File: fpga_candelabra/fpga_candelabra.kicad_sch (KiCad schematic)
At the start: 0 parts

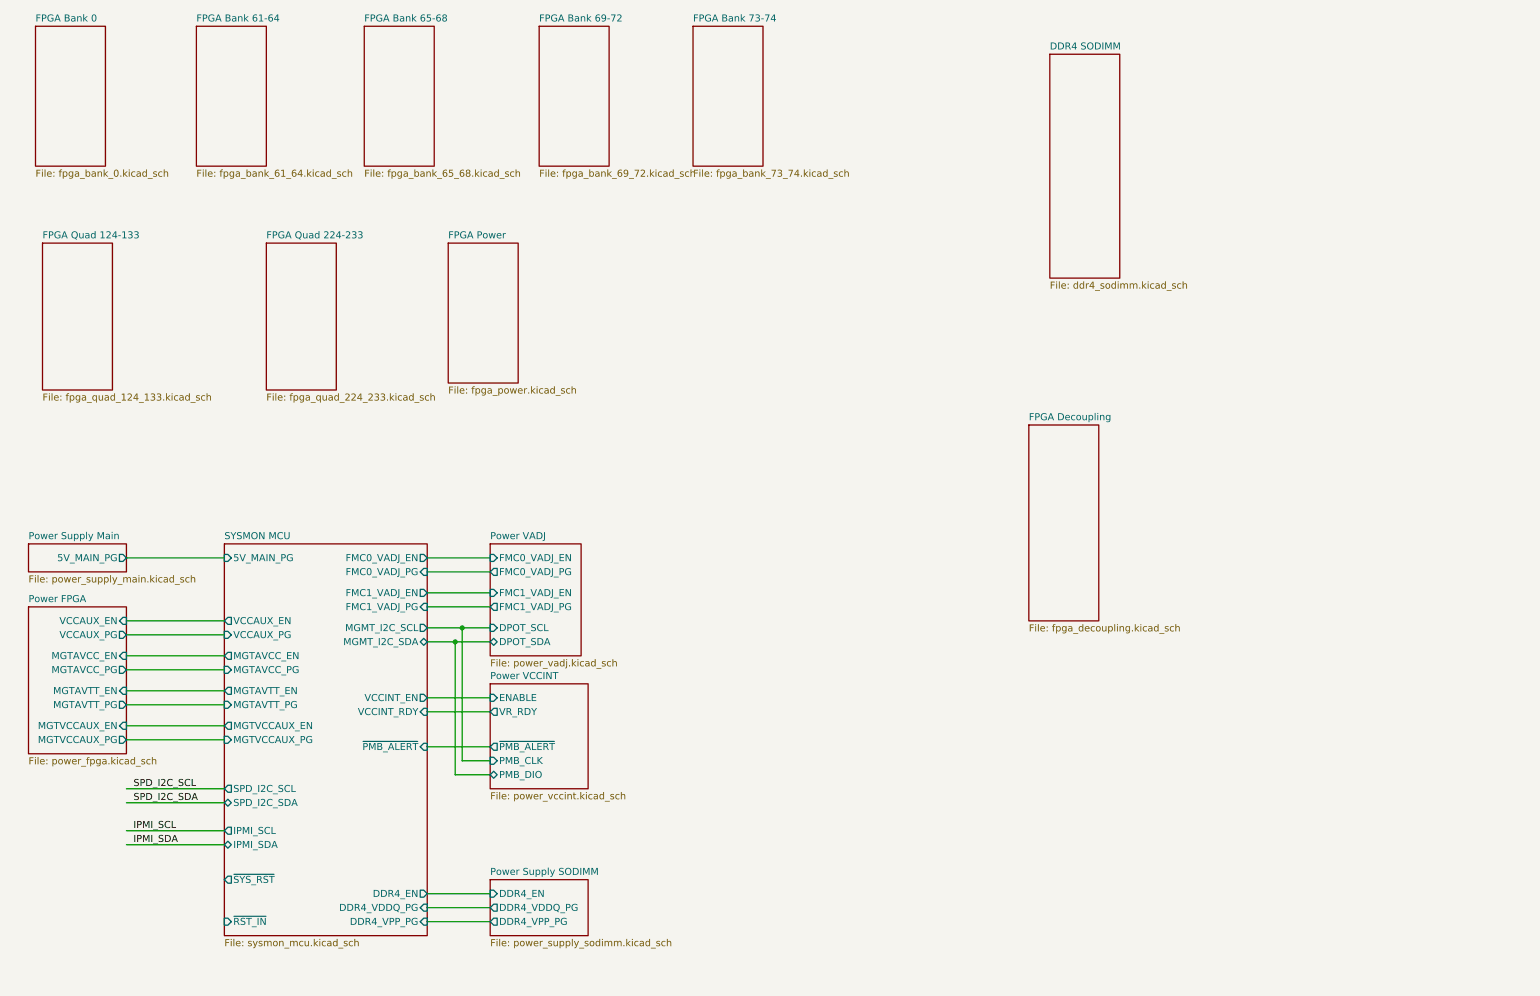
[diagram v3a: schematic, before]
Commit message: fpga_candelabra: reorganize fpga io and mgt by SLR
- Rename sch sheets
- Add prelimary DDR and PCIE Bank/Quad allocation

Signed-off-by: Yichuan Gao <gaoyichuan000@gmail.com>
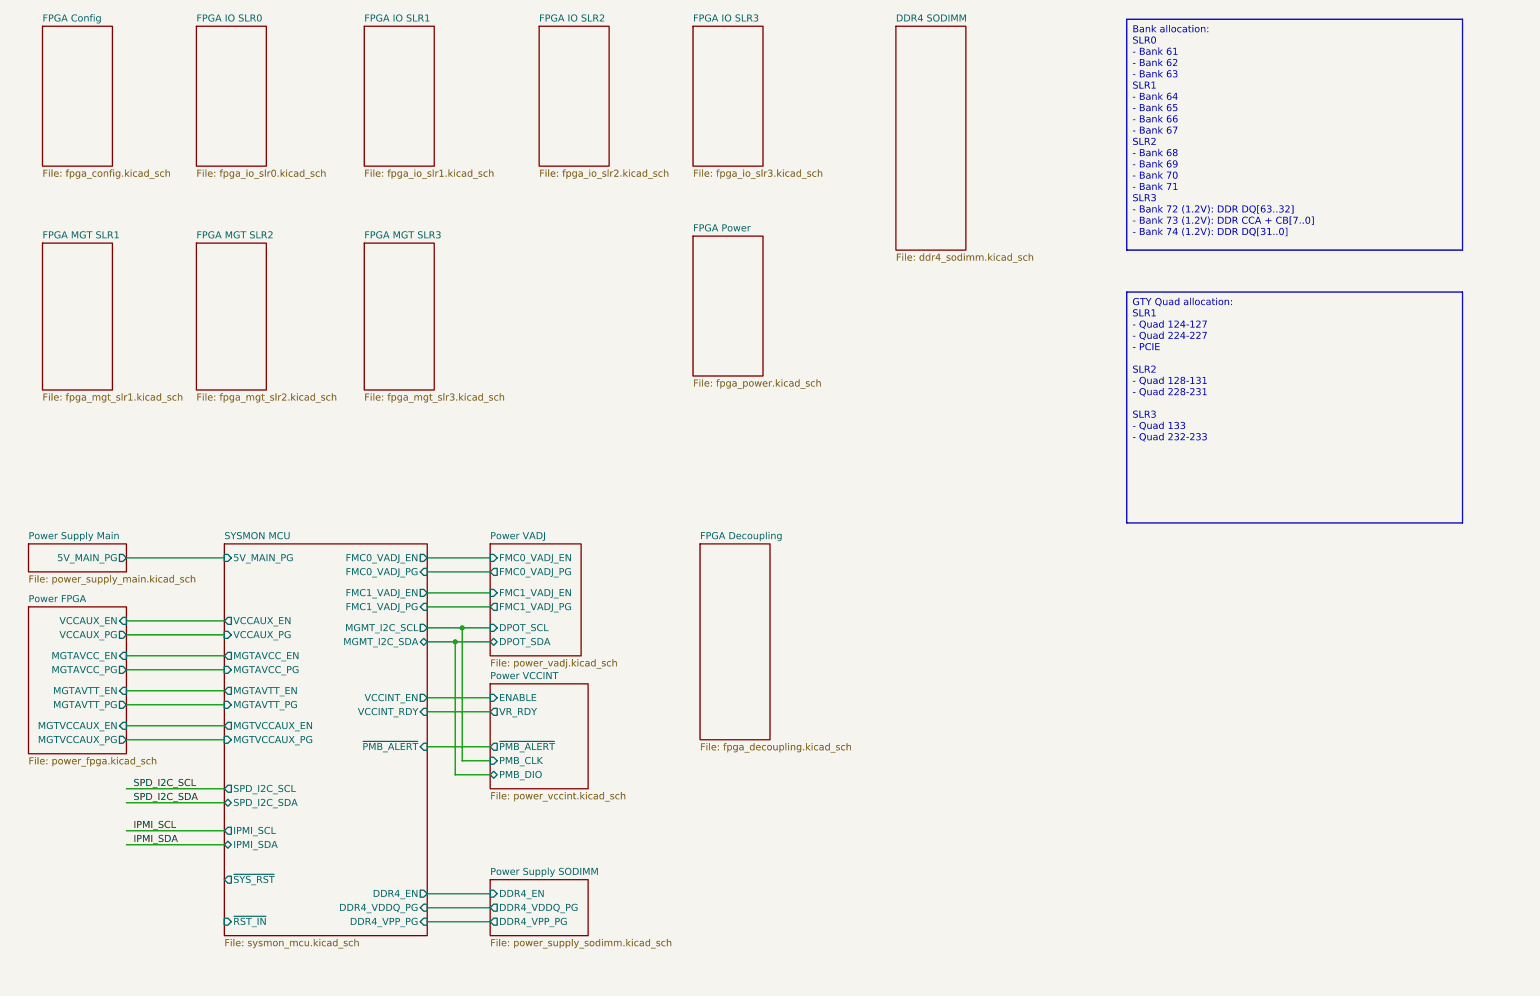
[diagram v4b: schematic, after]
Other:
- sheet FPGA Bank 0 renamed FPGA Config
- sheet FPGA Bank 61-64 renamed FPGA IO SLR0
- sheet FPGA Bank 65-68 renamed FPGA IO SLR1
- sheet FPGA Bank 69-72 renamed FPGA IO SLR2
- sheet FPGA Bank 73-74 renamed FPGA IO SLR3
- sheet FPGA Quad 124-133 renamed FPGA MGT SLR1
- sheet FPGA Quad 224-233 renamed FPGA MGT SLR2
- added sheet FPGA MGT SLR3 (fpga_mgt_slr3.kicad_sch)
- sheet FPGA Config: file fpga_bank_0.kicad_sch -> fpga_config.kicad_sch
- sheet FPGA IO SLR0: file fpga_bank_61_64.kicad_sch -> fpga_io_slr0.kicad_sch
- sheet FPGA IO SLR1: file fpga_bank_65_68.kicad_sch -> fpga_io_slr1.kicad_sch
- sheet FPGA IO SLR2: file fpga_bank_69_72.kicad_sch -> fpga_io_slr2.kicad_sch
- sheet FPGA IO SLR3: file fpga_bank_73_74.kicad_sch -> fpga_io_slr3.kicad_sch
- sheet FPGA MGT SLR1: file fpga_quad_124_133.kicad_sch -> fpga_mgt_slr1.kicad_sch
- sheet FPGA MGT SLR2: file fpga_quad_224_233.kicad_sch -> fpga_mgt_slr2.kicad_sch
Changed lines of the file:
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@@
 		)
 	)
-	(label "SPD_I2C_SDA"
-		(at 39.37 161.29 0)
-		(fields_autoplaced yes)
+	(text_box "Bank allocation:\nSLR0\n  - Bank 61\n  - Bank 62\n  - Bank 63\nSLR1\n  - Bank 64\n  - Bank 65\n  - Bank 66\n  - Bank 67\nSLR2\n  - Bank 68\n  - Bank 69\n  - Bank 70\n  - Bank 71\nSLR3\n  - Bank 72 (1.2V): DDR DQ[63..32]\n  - Bank 73 (1.2V): DDR CCA + CB[7..0]\n  - Bank 74 (1.2V): DDR DQ[31..0]"
+		(exclude_from_sim no)
+		(at 219.71 19.05 0)
+		(size 60.96 41.91)
+		(stroke
+			(width 0)
+			(type default)
+		)
+		(fill
+			(type none)
+		)
 		(effects
 			(font
 				(size 1.27 1.27)
 			)
-			(justify left bottom)
-		)
-	)
-	(label "IPMI_SCL"
-		(at 39.37 166.37 0)
-		(fields_autoplaced yes)
+			(justify left top)
+		)
+	)
+	(text_box "GTY Quad allocation:\nSLR1\n  - Quad 124-127\n  - Quad 224-227\n    - PCIE\n\nSLR2\n  - Quad 128-131\n  - Quad 228-231\n\nSLR3\n  - Quad 133\n  - Quad 232-233"
+		(exclude_from_sim no)
+		(at 219.71 68.58 0)
+		(size 60.96 41.91)
+		(stroke
+			(width 0)
+			(type default)
+		)
+		(fill
+			(type none)
+		)
 		(effects
 			(font
 				(size 1.27 1.27)
 			)
-			(justify left bottom)
-		)
-	)
-	(label "SPD_I2C_SCL"
-		(at 39.37 158.75 0)
+			(justify left top)
+		)
+	)
+	(label "SPD_I2C_SDA"
+		(at 39.37 161.29 0)
 		(fields_autoplaced yes)
 		(effects
@@
 		)
 	)
-	(label "IPMI_SDA"
-		(at 39.37 168.91 0)
+	(label "IPMI_SCL"
+		(at 39.37 166.37 0)
 		(fields_autoplaced yes)
 		(effects
@@
 		)
 	)
+	(label "SPD_I2C_SCL"
+		(at 39.37 158.75 0)
+		(fields_autoplaced yes)
+		(effects
+			(font
+				(size 1.27 1.27)
+			)
+			(justify left bottom)
+		)
+	)
+	(label "IPMI_SDA"
+		(at 39.37 168.91 0)
+		(fields_autoplaced yes)
+		(effects
+			(font
+				(size 1.27 1.27)
+			)
+			(justify left bottom)
+		)
+	)
 	(sheet
 		(at 113.03 20.32)
@@
 			(color 255 255 255 0.0000)
 		)
-		(property "Sheetname" "FPGA Bank 69-72"
+		(property "Sheetname" "FPGA IO SLR2"
 			(at 113.03 19.6084 0)
 			(effects
@@
 			)
 		)
-		(property "Sheetfile" "fpga_bank_69_72.kicad_sch"
+		(property "Sheetfile" "fpga_io_slr2.kicad_sch"
 			(at 113.03 46.3046 0)
 			(effects
@@
 			(project "fpga_candelabra"
 				(path "/01ed9e92-4e50-4b41-90dc-10444aaec5f7"
-					(page "15")
-				)
-			)
-		)
-	)
-	(sheet
-		(at 21.59 20.32)
+					(page "16")
+				)
+			)
+		)
+	)
+	(sheet
+		(at 22.86 20.32)
 		(size 12.7 25.4)
 		(fields_autoplaced yes)
@@
 			(color 255 255 255 0.0000)
 		)
-		(property "Sheetname" "FPGA Bank 0"
-			(at 21.59 19.6084 0)
-			(effects
-				(font
-					(size 1.27 1.27)
-				)
-				(justify left bottom)
-			)
-		)
-		(property "Sheetfile" "fpga_bank_0.kicad_sch"
-			(at 21.59 46.3046 0)
+		(property "Sheetname" "FPGA Config"
+			(at 22.86 19.6084 0)
+			(effects
+				(font
+					(size 1.27 1.27)
+				)
+				(justify left bottom)
+			)
+		)
+		(property "Sheetfile" "fpga_config.kicad_sch"
+			(at 22.86 46.3046 0)
 			(effects
 				(font
@@
 			(project "fpga_candelabra"
 				(path "/01ed9e92-4e50-4b41-90dc-10444aaec5f7"
-					(page "11")
+					(page "12")
+				)
+			)
+		)
+	)
+	(sheet
+		(at 81.28 59.69)
+		(size 12.7 26.67)
+		(fields_autoplaced yes)
+		(stroke
+			(width 0.1524)
+			(type solid)
+			(color 132 0 132 1)
+		)
+		(fill
+			(color 255 255 255 0.0000)
+		)
+		(property "Sheetname" "FPGA MGT SLR3"
+			(at 81.28 58.9784 0)
+			(effects
+				(font
+					(size 1.27 1.27)
+				)
+				(justify left bottom)
+			)
+		)
+		(property "Sheetfile" "fpga_mgt_slr3.kicad_sch"
+			(at 81.28 86.9446 0)
+			(effects
+				(font
+					(size 1.27 1.27)
+				)
+				(justify left top)
+			)
+		)
+		(instances
+			(project "fpga_candelabra"
+				(path "/01ed9e92-4e50-4b41-90dc-10444aaec5f7"
+					(page "9")
 				)
 			)
@@
 			(color 255 255 255 0.0000)
 		)
-		(property "Sheetname" "FPGA Quad 124-133"
+		(property "Sheetname" "FPGA MGT SLR1"
 			(at 22.86 58.9784 0)
 			(effects
@@
 			)
 		)
-		(property "Sheetfile" "fpga_quad_124_133.kicad_sch"
+		(property "Sheetfile" "fpga_mgt_slr1.kicad_sch"
 			(at 22.86 86.9446 0)
 			(effects
@@
 	)
 	(sheet
-		(at 201.93 92.71)
+		(at 142.24 114.3)
 		(size 12.7 35.56)
 		(fields_autoplaced yes)
@@
 		)
 		(property "Sheetname" "FPGA Decoupling"
-			(at 201.93 91.9984 0)
+			(at 142.24 113.5884 0)
 			(effects
 				(font
@@
 		)
 		(property "Sheetfile" "fpga_decoupling.kicad_sch"
-			(at 201.93 128.8546 0)
-			(effects
-				(font
-					(size 1.27 1.27)
-				)
-				(justify left top)
-			)
-		)
-		(instances
-			(project "fpga_candelabra"
-				(path "/01ed9e92-4e50-4b41-90dc-10444aaec5f7"
-					(page "16")
+			(at 142.24 150.4446 0)
+			(effects
+				(font
+					(size 1.27 1.27)
+				)
+				(justify left top)
+			)
+		)
+		(instances
+			(project "fpga_candelabra"
+				(path "/01ed9e92-4e50-4b41-90dc-10444aaec5f7"
+					(page "17")
 				)
 			)
@@
 			(color 255 255 255 0.0000)
 		)
-		(property "Sheetname" "FPGA Bank 65-68"
+		(property "Sheetname" "FPGA IO SLR1"
 			(at 81.28 19.6084 0)
 			(effects
@@
 			)
 		)
-		(property "Sheetfile" "fpga_bank_65_68.kicad_sch"
+		(property "Sheetfile" "fpga_io_slr1.kicad_sch"
 			(at 81.28 46.3046 0)
 			(effects
@@
 			(color 255 255 255 0.0000)
 		)
-		(property "Sheetname" "FPGA Bank 73-74"
+		(property "Sheetname" "FPGA IO SLR3"
 			(at 140.97 19.6084 0)
 			(effects
@@
 			)
 		)
-		(property "Sheetfile" "fpga_bank_73_74.kicad_sch"
+		(property "Sheetfile" "fpga_io_slr3.kicad_sch"
 			(at 140.97 46.3046 0)
 			(effects
@@
 			(project "fpga_candelabra"
 				(path "/01ed9e92-4e50-4b41-90dc-10444aaec5f7"
-					(page "10")
+					(page "11")
 				)
 			)
@@
 			(color 255 255 255 0.0000)
 		)
-		(property "Sheetname" "FPGA Bank 61-64"
+		(property "Sheetname" "FPGA IO SLR0"
 			(at 50.8 19.6084 0)
 			(effects
@@
 			)
 		)
-		(property "Sheetfile" "fpga_bank_61_64.kicad_sch"
+		(property "Sheetfile" "fpga_io_slr0.kicad_sch"
 			(at 50.8 46.3046 0)
 			(effects
@@
 			(project "fpga_candelabra"
 				(path "/01ed9e92-4e50-4b41-90dc-10444aaec5f7"
-					(page "13")
-				)
-			)
-		)
-	)
-	(sheet
-		(at 96.52 59.69)
+					(page "14")
+				)
+			)
+		)
+	)
+	(sheet
+		(at 140.97 58.42)
 		(size 12.7 25.4)
 		(fields_autoplaced yes)
@@
 		)
 		(property "Sheetname" "FPGA Power"
-			(at 96.52 58.9784 0)
+			(at 140.97 57.7084 0)
 			(effects
 				(font
@@
 		)
 		(property "Sheetfile" "fpga_power.kicad_sch"
-			(at 96.52 85.6746 0)
-			(effects
-				(font
-					(size 1.27 1.27)
-				)
-				(justify left top)
-			)
-		)
-		(instances
-			(project "fpga_candelabra"
-				(path "/01ed9e92-4e50-4b41-90dc-10444aaec5f7"
-					(page "9")
+			(at 140.97 84.4046 0)
+			(effects
+				(font
+					(size 1.27 1.27)
+				)
+				(justify left top)
+			)
+		)
+		(instances
+			(project "fpga_candelabra"
+				(path "/01ed9e92-4e50-4b41-90dc-10444aaec5f7"
+					(page "10")
 				)
 			)
@@
 			(project "fpga_candelabra"
 				(path "/01ed9e92-4e50-4b41-90dc-10444aaec5f7"
-					(page "12")
-				)
-			)
-		)
-	)
-	(sheet
-		(at 205.74 25.4)
+					(page "13")
+				)
+			)
+		)
+	)
+	(sheet
+		(at 177.8 20.32)
 		(size 12.7 40.64)
 		(fields_autoplaced yes)
@@
 		)
 		(property "Sheetname" "DDR4 SODIMM"
-			(at 205.74 24.6884 0)
+			(at 177.8 19.6084 0)
 			(effects
 				(font
@@
 		)
 		(property "Sheetfile" "ddr4_sodimm.kicad_sch"
-			(at 205.74 66.6246 0)
-			(effects
-				(font
-					(size 1.27 1.27)
-				)
-				(justify left top)
-			)
-		)
-		(instances
-			(project "fpga_candelabra"
-				(path "/01ed9e92-4e50-4b41-90dc-10444aaec5f7"
-					(page "17")
+			(at 177.8 61.5446 0)
+			(effects
+				(font
+					(size 1.27 1.27)
+				)
+				(justify left top)
+			)
+		)
+		(instances
+			(project "fpga_candelabra"
+				(path "/01ed9e92-4e50-4b41-90dc-10444aaec5f7"
+					(page "18")
 				)
 			)
@@
 			(project "fpga_candelabra"
 				(path "/01ed9e92-4e50-4b41-90dc-10444aaec5f7"
-					(page "14")
-				)
-			)
-		)
-	)
-	(sheet
-		(at 63.5 59.69)
+					(page "15")
+				)
+			)
+		)
+	)
+	(sheet
+		(at 50.8 59.69)
 		(size 12.7 26.67)
 		(fields_autoplaced yes)
@@
 			(color 255 255 255 0.0000)
 		)
-		(property "Sheetname" "FPGA Quad 224-233"
-			(at 63.5 58.9784 0)
-			(effects
-				(font
-					(size 1.27 1.27)
-				)
-				(justify left bottom)
-			)
-		)
-		(property "Sheetfile" "fpga_quad_224_233.kicad_sch"
-			(at 63.5 86.9446 0)
-			(effects
-				(font
+		(property "Sheetname" "FPGA MGT SLR2"
+			(at 50.8 58.9784 0)
+			(effects
+				(font
+					(size 1.27 1.27)
+				)
+				(justify left bottom)
+			)
+		)
+		(property "Sheetfile" "fpga_mgt_slr2.kicad_sch"
+			(at 50.8 86.9446 0)
+			(effects
+				(font
